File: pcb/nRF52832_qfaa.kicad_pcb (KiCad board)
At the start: 4 copper layers, 41.5 x 13 mm, 77 parts, among them J1 Conn_01x01_Female, J2 Conn_02x05_Odd_Even, U1 NRF52832, U2 W25Q32JVZP, U3 TLV75533PDBVR, U4 BQ24078RGTR, X1 32.768kHz, X2 32MHz

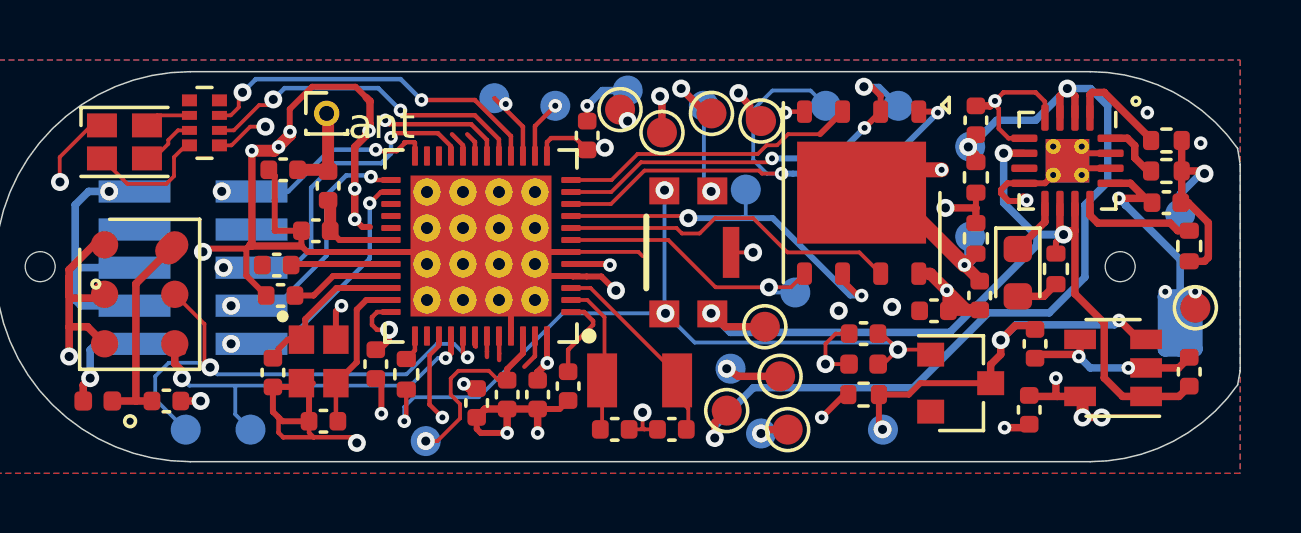
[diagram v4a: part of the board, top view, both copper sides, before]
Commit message: [pcb] finalizing layout of v1.3, only testpoints, teardrops and DRC is left
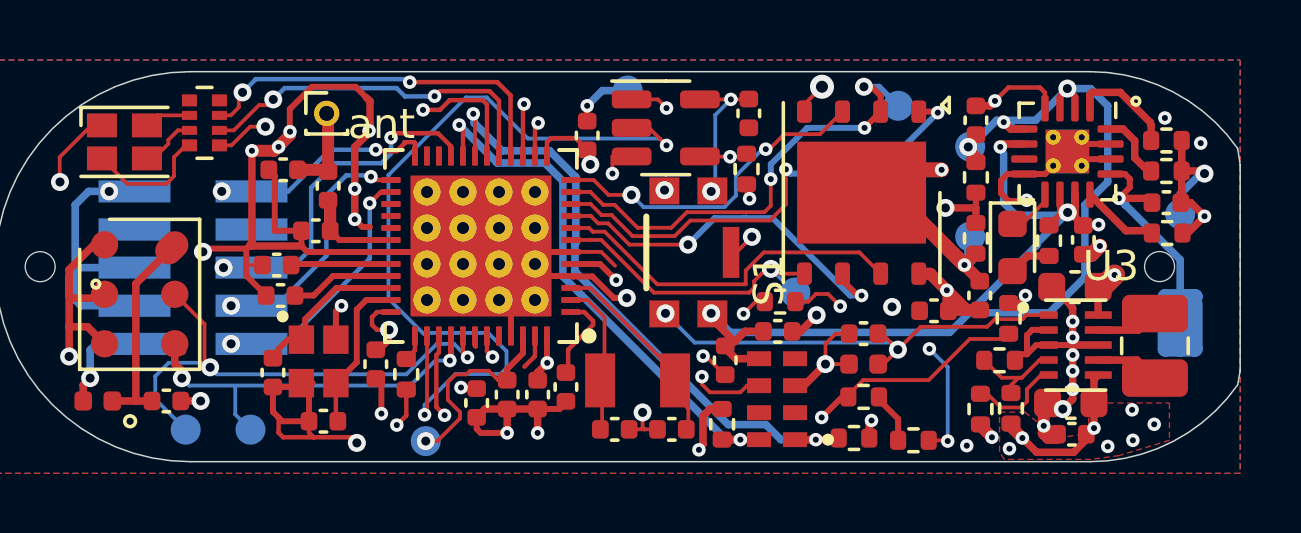
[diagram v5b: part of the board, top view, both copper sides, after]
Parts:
- removed D2: BAS40-05,215, Package_TO_SOT_SMD:SOT-23
- removed TP13, TP15, TP16, TP17, TP18, TP19, TP20, TP21, TP22, TP23, TP24, TP25, TP26, TP27, TP28, TP6, TP7: TestPoint, TestPoint:TestPoint_Pad_D1.0mm
- added C2: 22uF, Capacitor_SMD:C_0603_1608Metric, F.Cu at (65.3, 39.9)
- added C24: 1uF, Capacitor_SMD:C_0402_1005Metric, F.Cu at (53.8, 38.5)
- added C25: 100nF, Capacitor_SMD:C_0402_1005Metric, F.Cu at (55.5, 37.5)
- added C26: 1uF, Capacitor_SMD:C_0402_1005Metric, F.Cu at (54.6, 30.2)
- added L1: 0.47uH, Inductor_SMD:L_1008_2520Metric, F.Cu at (68.1, 38.0)
- added R12: 33, Resistor_SMD:R_0402_1005Metric, F.Cu at (55.6, 36.5)
- added R14: 100k, Resistor_SMD:R_0402_1005Metric, F.Cu at (62.3, 40.1)
- added R15: 511k, Resistor_SMD:R_0402_1005Metric, F.Cu at (63.3, 40.1)
- added R16: 91k, Resistor_SMD:R_0402_1005Metric, F.Cu at (62.9, 38.5)
- added R17: 1.6K, Resistor_SMD:R_0402_1005Metric, F.Cu at (54.5, 32.1)
- added R2: 4.7k, Resistor_SMD:R_0402_1005Metric, F.Cu at (58.1, 41.0)
- added R4: 4.7k, Resistor_SMD:R_0402_1005Metric, F.Cu at (53.7, 40.6)
- added R5: 1.6K, Resistor_SMD:R_0402_1005Metric, F.Cu at (63.2, 37.1)
- added R_DNP_1: 1.6K, Resistor_SMD:R_0402_1005Metric, F.Cu at (60.1, 41.1)
- added U5: RV-4162-C7, _other:IC_RV-4162-C7, F.Cu at (55.5, 39.8)
- added U6: SN74LVC1G79DBVT, Package_TO_SOT_SMD:SOT-23-5, F.Cu at (51.8, 30.7)
- C1: value 10uF -> 22uF; footprint Capacitor_SMD:C_0402_1005Metric -> Capacitor_SMD:C_0603_1608Metric
- C23: value 100pF -> 10uF
- U3: value TLV75533PDBVR -> TPS63802DLAR; footprint Package_TO_SOT_SMD:SOT-23-5 -> _other:VREG_TPS63802DLAR
- moved C21 5.64 mm to (65.7, 34.4), turned to -90 degrees
- moved C1 4.36 mm to (65.5, 36.0), turned to 180 degrees
- moved C23 3.25 mm to (65.4, 40.9), turned to 180 degrees
- moved U3 1.46 mm to (65.5, 37.9), turned to 0 degrees
- moved H1 1.31 mm to (68.3, 35.3)
- moved R9 0.97 mm to (64.6, 34.5)
- moved D3 0.86 mm to (63.4, 34.7)
- moved R8 0.85 mm to (68.5, 34.2), turned to 0 degrees
- moved U4 0.31 mm to (65.2, 31.5)
- moved C9 0.08 mm to (48.5, 39.3)
- moved R5 0.08 mm to (58.4, 39.7)
- moved X1 0.07 mm to (50.9, 39.1)
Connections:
- C1 pad 1: VCC -> VSS
- C23 pad 1: /Power/LDO_EN -> VCC
- U1 pad 19: /P0.16 -> /I2C_SDA
- U1 pad 20: /P0.17 -> /I2C_SCL
- U1 pad 38: unconnected-(U1-Pad38) -> FF_CLK
- U1 pad 43: unconnected-(U1-Pad43) -> /RTC_INT_N
- U3 pad 1: VSS -> MAIN_BUTTON
- U3 pad 3: /Power/LDO_EN -> GND
- U3 pad 4: GND -> Net-(R15-Pad2)
- U3 pad 5: VCC -> Net-(R14-Pad2)
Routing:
- net FF_CLK: track 0.00 -> 28.1 mm, vias 0 -> 2
- net /I2C_SDA: track 0.00 -> 20.9 mm, vias 0 -> 2
- net /I2C_SCL: track 0.00 -> 17.9 mm, vias 0 -> 2
- net /Power/FF_D: track 0.00 -> 16.7 mm, vias 0 -> 2
- net /Power/FF_Q: track 0.00 -> 16.0 mm, vias 0 -> 3
- net +BATT: track 30.8 -> 19.2 mm
- net /Power/LDO_EN: track 13.5 -> 2.01 mm, vias 3 -> 0
- net /RTC_INT_N: track 0.00 -> 10.6 mm, vias 0 -> 2
- net Net-(R12-Pad2): track 0.00 -> 10.2 mm, vias 0 -> 2
- net VSS: track 39.9 -> 49.1 mm, vias 4 -> 8
- net MCU_POWER_LATCH: track 17.1 -> 23.0 mm
- net GND: track 122.1 -> 127.7 mm, vias 35 -> 41
- net MAIN_BUTTON: track 27.1 -> 31.7 mm, vias 4 -> 5
- net /MEM_CS: track 19.9 -> 15.8 mm
- net Net-(R15-Pad2): track 0.00 -> 3.32 mm
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- added copper zone on F.Cu, net VCC

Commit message: [pcb] finalized layout of v1.3
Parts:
- removed the C2 at (45.5, 39.9)
- removed the R5 at (58.4, 39.7)
- removed R_DNP_1: 1.6K, Resistor_SMD:R_0402_1005Metric
- removed TP12, TP14: TestPoint, TestPoint:TestPoint_Pad_D1.0mm
- added TP16: TestPoint, TestPoint:TestPoint_Pad_D1.0mm, B.Cu at (59.8, 39.2)
- added TP18: TestPoint, TestPoint:TestPoint_Pad_D1.0mm, B.Cu at (55.9, 39.4)
- added TP19: TestPoint, TestPoint:TestPoint_Pad_D1.0mm, B.Cu at (34.7, 30.2)
- added TP24: TestPoint, TestPoint:TestPoint_Pad_D1.0mm, B.Cu at (63.2, 40.1)
- added TP25: TestPoint, TestPoint:TestPoint_Pad_D1.0mm, B.Cu at (67.5, 40.4)
- added TP26: TestPoint, TestPoint:TestPoint_Pad_D1.0mm, B.Cu at (67.0, 37.2)
- added TP27: TestPoint, TestPoint:TestPoint_Pad_D1.0mm, B.Cu at (66.7, 29.7)
- added TP28: TestPoint, TestPoint:TestPoint_Pad_D1.0mm, B.Cu at (46.6, 40.8)
- added TP5: TestPoint, TestPoint:TestPoint_Pad_D1.0mm, B.Cu at (49.9, 40.8)
- added TP6: TestPoint, TestPoint:TestPoint_Pad_D1.0mm, B.Cu at (52.6, 31.0)
- added TP7: TestPoint, TestPoint:TestPoint_Pad_D1.0mm, B.Cu at (48.2, 29.7)
- moved H1 0.39 mm to (67.9, 35.4)
- moved TP11 0.15 mm to (43.8, 41.0)
- moved C17 0.13 mm to (62.2, 36.3)
- moved R12 0.09 mm to (55.6, 36.6)
- moved R17 0.08 mm to (54.4, 32.1)
- moved R9 0.06 mm to (64.6, 34.4)
- moved U4 0.05 mm to (65.2, 31.4)
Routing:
- net +BATT: track 19.2 -> 8.34 mm
- net /P0.12: track 1.75 -> 7.98 mm
- net /I2C_SCL: track 17.9 -> 21.9 mm
- net V_charger: track 14.4 -> 16.5 mm
- net VSS: track 49.1 -> 51.1 mm
- net /Power/LDO_EN: track 2.01 -> 0.00 mm
- net MAIN_BUTTON: track 31.7 -> 33.1 mm
- net GND: track 127.7 -> 129.1 mm, vias 41 -> 40
- net /P0.11: track 1.15 -> 2.27 mm
- net /I2C_SDA: track 20.9 -> 21.8 mm
- net VCC: track 90.0 -> 89.2 mm
- net FF_CLK: track 28.1 -> 27.5 mm
- net MCU_POWER_LATCH: track 23.0 -> 23.5 mm
- net /DEC4: track 6.97 -> 6.46 mm
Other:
- board text removed: "gnd"
- board text removed: "rx"
- board text removed: "tx"

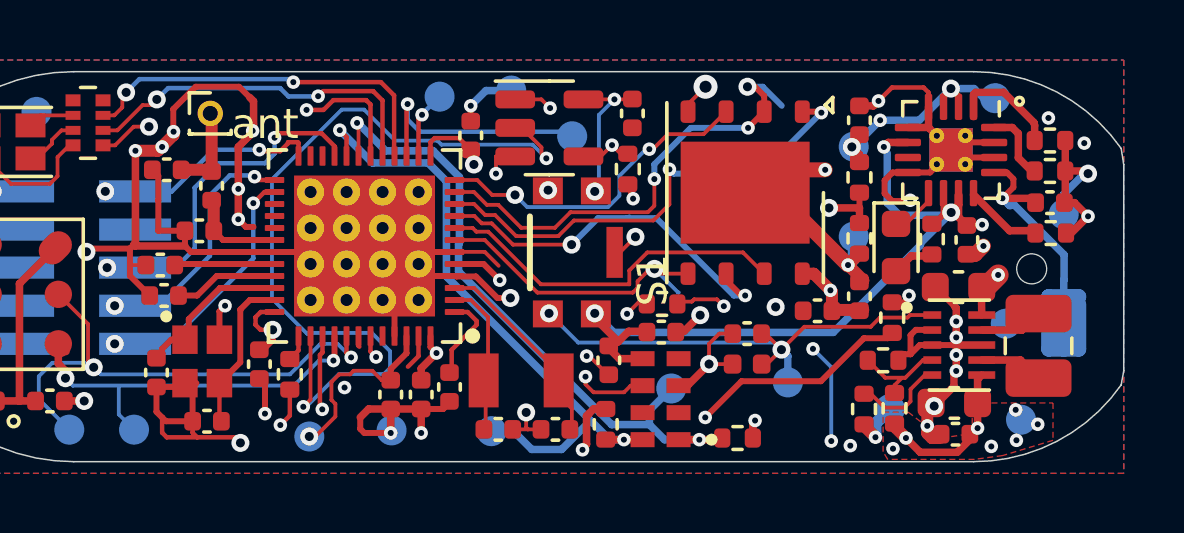
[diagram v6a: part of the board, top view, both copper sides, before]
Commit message: [pcb] finalized 1.3: added testpoints, fixed DRC errors
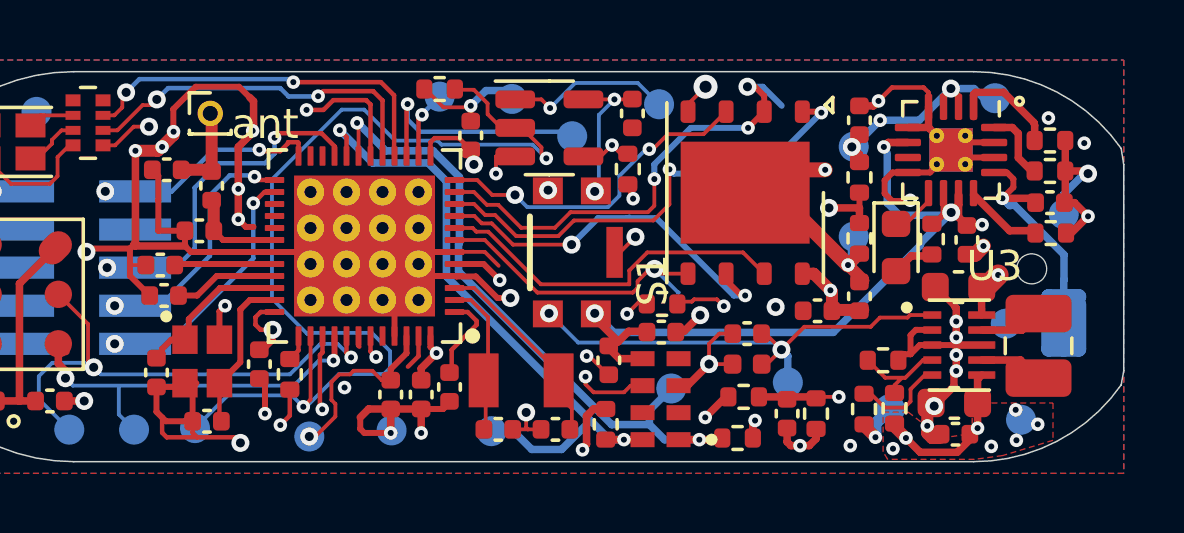
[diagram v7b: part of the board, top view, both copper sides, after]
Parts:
- added C27: 100nF, Capacitor_SMD:C_0402_1005Metric, F.Cu at (59.7, 40.2)
- added R18: 100K, Resistor_SMD:R_0402_1005Metric, F.Cu at (60.7, 40.2)
- added R19: 100K, Resistor_SMD:R_0402_1005Metric, F.Cu at (48.2, 29.4)
- added TP12: TestPoint, TestPoint:TestPoint_Pad_D1.0mm, B.Cu at (55.5, 29.9)
- added TP13: TestPoint, TestPoint:TestPoint_Pad_D1.0mm, B.Cu at (40.0, 40.7)
- moved R5 5.61 mm to (58.3, 39.7), turned to 180 degrees
- moved TP8 0.28 mm to (50.6, 29.7)
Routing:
- net /Power/FF_Q: track 15.8 -> 1.89 mm, vias 3 -> 1
- net /Power/FF_D: track 16.7 -> 24.8 mm
- net FF_CLK: track 27.5 -> 34.4 mm
- net MCU_POWER_LATCH: track 23.5 -> 17.2 mm
- net GND: track 129.1 -> 132.7 mm, vias 40 -> 41

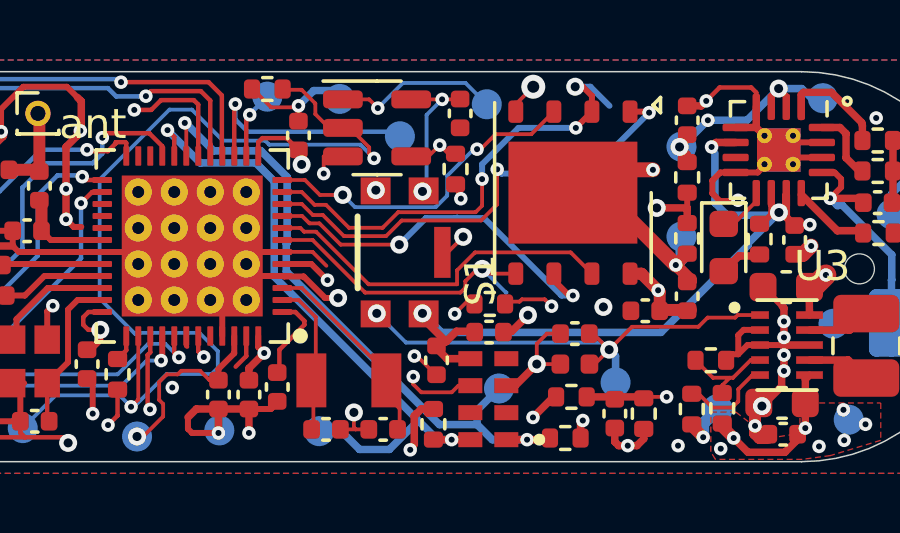
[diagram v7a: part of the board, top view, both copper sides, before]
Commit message: [pcb] finalized main work on fixture 1.3
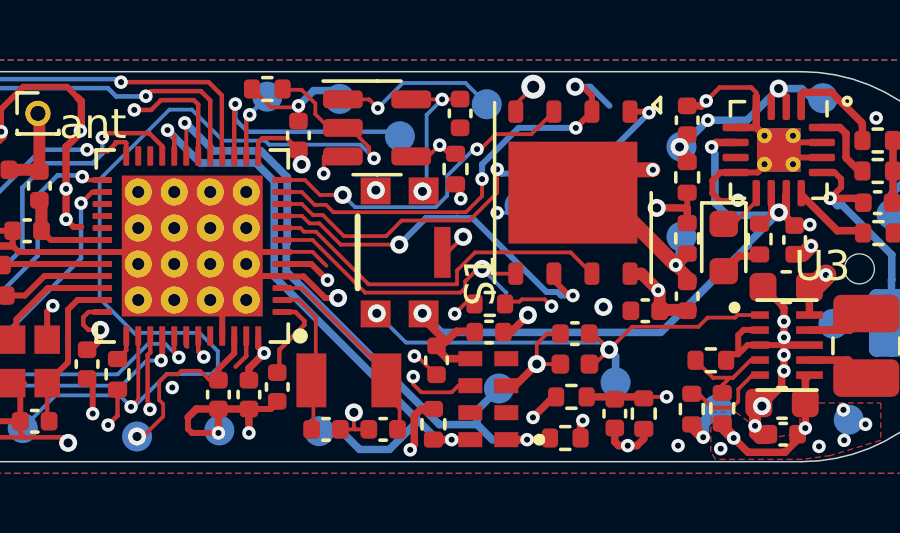
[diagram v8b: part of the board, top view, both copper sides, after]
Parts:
- added TP14: TestPoint, TestPoint:TestPoint_Pad_D1.0mm, B.Cu at (56.6, 33.3)
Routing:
- net /Power/FF_Q: track 1.89 -> 6.10 mm, vias 1 -> 2
- net /MEM_DO: track 15.9 -> 15.2 mm
